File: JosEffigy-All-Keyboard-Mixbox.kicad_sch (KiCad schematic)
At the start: 33 parts, among them U1 Pico

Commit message: Release 1.0b
Moved power to VBUS, added DTranslator, added Capacitors
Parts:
- added C1, C10, C11, C12, C13, C14, C15, C16, C2, C3, C4, C5, C6, C7, C8, C9: 100nf, CAPC1005X55N:CAPC1005X55N, symbol Device:C_Small
- added U2: SN74LV1T34DBV, Package_TO_SOT_SMD:SOT-23-5, symbol Logic_LevelTranslator:SN74LV1T34DBV
- MX8: footprint Button_Switch_Keyboard:SW_Cherry_MX_2.00u_Plate -> PCM_Switch_Keyboard_Hotswap_Kailh:SW_Hotswap_Kailh_MX_Plated_2.00u
- U1: footprint RPi_Pico:RPi_Pico_SMD_TH -> MCU_RaspberryPi_and_Boards:RPi_Pico_SMD_TH
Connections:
- net GND: now also U1.38 (GND), C1.2, C10.2, C11.2, C12.2, C13.2, C14.2, C15.2, C16.2, C2.2, C3.2, C4.2, C5.2, C6.2, C7.2, C8.2, C9.2, U2.3 (GND)
- net RGB0: now also U2.2 (A); no longer D1.3 (DIN)
- net VCC: now also U1.40 (VBUS), C1.1, C10.1, C11.1, C12.1, C13.1, C14.1, C15.1, C16.1, C2.1, C3.1, C4.1, C5.1, C6.1, C7.1, C8.1, C9.1, U2.5 (VCC); no longer U1.36 (3V3)
- net at D13.1 (DOUT): no longer D14.3 (DIN)
- net at D13.3 (DIN): now also D14.1 (DOUT); no longer D12.1 (DOUT)
- net at D16.3 (DIN): now also D12.1 (DOUT); no longer D15.1 (DOUT)
- net at D15.3 (DIN): now also D16.1 (DOUT); no longer D14.1 (DOUT)
- new net: D1.3 (DIN), U2.4 (Y)
- new net: D14.3 (DIN), D15.1 (DOUT)

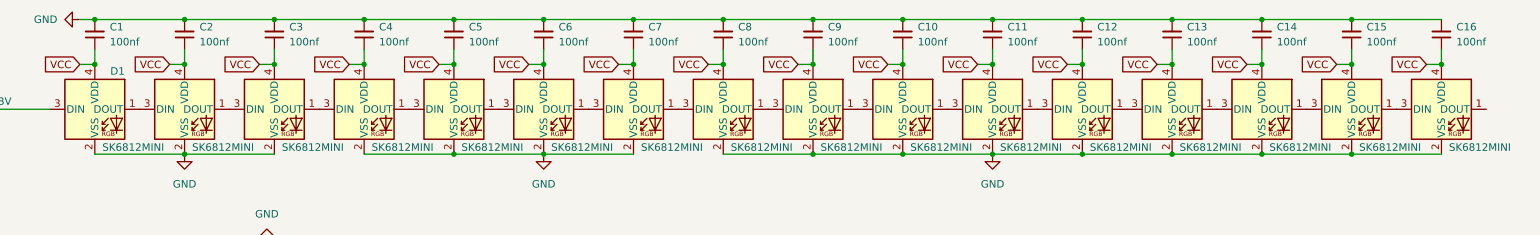
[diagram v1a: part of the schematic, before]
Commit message: Release 1.0c
redid the routing
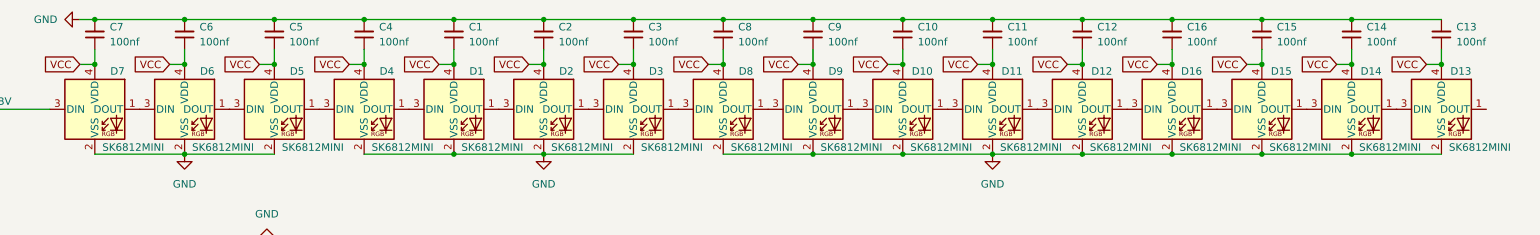
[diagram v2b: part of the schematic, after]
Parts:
- removed D7: SK6812MINI, kicad-footprints:YS-SK6812MINI-E, symbol LED:SK6812MINI
- added D1: SK6812MINI, kicad-footprints:YS-SK6812MINI-E, symbol LED:SK6812MINI
- renumbered C5 to C1, C16 to C13, C15 to C14, C14 to C15, C13 to C16, C6 to C2, C7 to C3, C3 to C5, C2 to C6, C1 to C7, D1 to D7
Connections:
- net GND: now also D1.2 (VSS)
- net VCC: now also D1.4 (VDD)
- net at D8.3 (DIN): now also D3.1 (DOUT)
- net at D7.1 (DOUT): now also D6.3 (DIN); no longer D2.3 (DIN)
- net at D5.3 (DIN): now also D6.1 (DOUT); no longer D4.1 (DOUT)
- net at D4.3 (DIN): now also D5.1 (DOUT); no longer D3.1 (DOUT)
- new net: D1.3 (DIN), D4.1 (DOUT)
- new net: D1.1 (DOUT), D2.3 (DIN)

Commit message: Release 1.1b
Update just to be sure
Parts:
- MX1, MX10, MX11, MX12, MX13, MX14, MX15, MX16, MX2, MX3, MX4, MX5, MX6, MX7, MX9: footprint PCM_Switch_Keyboard_Hotswap_Kailh:SW_Hotswap_Kailh_MX_Plated_1.00u -> Kailh:Kailh_socket_PG1350_optional
- MX8: footprint PCM_Switch_Keyboard_Hotswap_Kailh:SW_Hotswap_Kailh_MX_Plated_2.00u -> Kailh:Kailh_socket_PG1350_optional
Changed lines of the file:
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@@
       (effects (font (size 0.508 0.508)))
     )
-    (property "Footprint" "PCM_Switch_Keyboard_Hotswap_Kailh:SW_Hotswap_Kailh_MX_Plated_1.00u" (at 109.855 62.865 0)
+    (property "Footprint" "Kailh:Kailh_socket_PG1350_optional" (at 109.855 62.865 0)
       (effects (font (size 1.524 1.524)) hide)
     )
@@
       (effects (font (size 0.508 0.508)))
     )
-    (property "Footprint" "PCM_Switch_Keyboard_Hotswap_Kailh:SW_Hotswap_Kailh_MX_Plated_1.00u" (at 198.755 100.965 0)
+    (property "Footprint" "Kailh:Kailh_socket_PG1350_optional" (at 198.755 100.965 0)
       (effects (font (size 1.524 1.524)) hide)
     )
@@
       (effects (font (size 0.508 0.508)))
     )
-    (property "Footprint" "PCM_Switch_Keyboard_Hotswap_Kailh:SW_Hotswap_Kailh_MX_Plated_1.00u" (at 224.155 88.265 0)
+    (property "Footprint" "Kailh:Kailh_socket_PG1350_optional" (at 224.155 88.265 0)
       (effects (font (size 1.524 1.524)) hide)
     )
@@
       (effects (font (size 0.508 0.508)))
     )
-    (property "Footprint" "PCM_Switch_Keyboard_Hotswap_Kailh:SW_Hotswap_Kailh_MX_Plated_1.00u" (at 224.155 100.965 0)
+    (property "Footprint" "Kailh:Kailh_socket_PG1350_optional" (at 224.155 100.965 0)
       (effects (font (size 1.524 1.524)) hide)
     )
@@
       (effects (font (size 0.508 0.508)))
     )
-    (property "Footprint" "PCM_Switch_Keyboard_Hotswap_Kailh:SW_Hotswap_Kailh_MX_Plated_1.00u" (at 135.255 62.865 0)
+    (property "Footprint" "Kailh:Kailh_socket_PG1350_optional" (at 135.255 62.865 0)
       (effects (font (size 1.524 1.524)) hide)
     )
@@
       (effects (font (size 0.508 0.508)))
     )
-    (property "Footprint" "PCM_Switch_Keyboard_Hotswap_Kailh:SW_Hotswap_Kailh_MX_Plated_1.00u" (at 186.055 100.965 0)
+    (property "Footprint" "Kailh:Kailh_socket_PG1350_optional" (at 186.055 100.965 0)
       (effects (font (size 1.524 1.524)) hide)
     )
@@
       (effects (font (size 0.508 0.508)))
     )
-    (property "Footprint" "PCM_Switch_Keyboard_Hotswap_Kailh:SW_Hotswap_Kailh_MX_Plated_1.00u" (at 109.855 100.965 0)
+    (property "Footprint" "Kailh:Kailh_socket_PG1350_optional" (at 109.855 100.965 0)
       (effects (font (size 1.524 1.524)) hide)
     )
@@
       (effects (font (size 0.508 0.508)))
     )
-    (property "Footprint" "PCM_Switch_Keyboard_Hotswap_Kailh:SW_Hotswap_Kailh_MX_Plated_1.00u" (at 122.555 100.965 0)
+    (property "Footprint" "Kailh:Kailh_socket_PG1350_optional" (at 122.555 100.965 0)
       (effects (font (size 1.524 1.524)) hide)
     )
@@
       (effects (font (size 0.508 0.508)))
     )
-    (property "Footprint" "PCM_Switch_Keyboard_Hotswap_Kailh:SW_Hotswap_Kailh_MX_Plated_1.00u" (at 122.555 88.265 0)
+    (property "Footprint" "Kailh:Kailh_socket_PG1350_optional" (at 122.555 88.265 0)
       (effects (font (size 1.524 1.524)) hide)
     )
@@
       (effects (font (size 0.508 0.508)))
     )
-    (property "Footprint" "PCM_Switch_Keyboard_Hotswap_Kailh:SW_Hotswap_Kailh_MX_Plated_1.00u" (at 186.055 88.265 0)
+    (property "Footprint" "Kailh:Kailh_socket_PG1350_optional" (at 186.055 88.265 0)
       (effects (font (size 1.524 1.524)) hide)
     )
@@
       (effects (font (size 0.508 0.508)))
     )
-    (property "Footprint" "PCM_Switch_Keyboard_Hotswap_Kailh:SW_Hotswap_Kailh_MX_Plated_1.00u" (at 211.455 88.265 0)
+    (property "Footprint" "Kailh:Kailh_socket_PG1350_optional" (at 211.455 88.265 0)
       (effects (font (size 1.524 1.524)) hide)
     )
@@
       (effects (font (size 0.508 0.508)))
     )
-    (property "Footprint" "PCM_Switch_Keyboard_Hotswap_Kailh:SW_Hotswap_Kailh_MX_Plated_1.00u" (at 198.755 88.265 0)
+    (property "Footprint" "Kailh:Kailh_socket_PG1350_optional" (at 198.755 88.265 0)
       (effects (font (size 1.524 1.524)) hide)
     )
@@
       (effects (font (size 0.508 0.508)))
     )
-    (property "Footprint" "PCM_Switch_Keyboard_Hotswap_Kailh:SW_Hotswap_Kailh_MX_Plated_1.00u" (at 211.455 100.965 0)
+    (property "Footprint" "Kailh:Kailh_socket_PG1350_optional" (at 211.455 100.965 0)
       (effects (font (size 1.524 1.524)) hide)
     )
@@
       (effects (font (size 0.508 0.508)))
     )
-    (property "Footprint" "PCM_Switch_Keyboard_Hotswap_Kailh:SW_Hotswap_Kailh_MX_Plated_1.00u" (at 122.555 62.865 0)
+    (property "Footprint" "Kailh:Kailh_socket_PG1350_optional" (at 122.555 62.865 0)
       (effects (font (size 1.524 1.524)) hide)
     )
@@
       (effects (font (size 0.508 0.508)))
     )
-    (property "Footprint" "PCM_Switch_Keyboard_Hotswap_Kailh:SW_Hotswap_Kailh_MX_Plated_1.00u" (at 135.255 100.965 0)
+    (property "Footprint" "Kailh:Kailh_socket_PG1350_optional" (at 135.255 100.965 0)
       (effects (font (size 1.524 1.524)) hide)
     )
@@
       (effects (font (size 0.508 0.508)))
     )
-    (property "Footprint" "PCM_Switch_Keyboard_Hotswap_Kailh:SW_Hotswap_Kailh_MX_Plated_2.00u" (at 160.655 113.665 0)
-      (effects (font (size 1.524 1.524)) hide)
-    )
+    (property "Footprint" "Kailh:Kailh_socket_PG1350_optional" (at 160.655 113.665 0)
+      (effects (font (size 1.524 1.524)) hide)
+    )

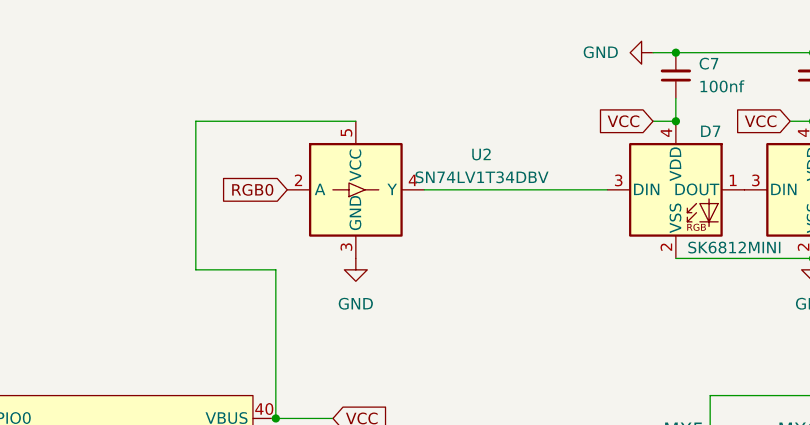
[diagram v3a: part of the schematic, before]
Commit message: Redid all routing manually
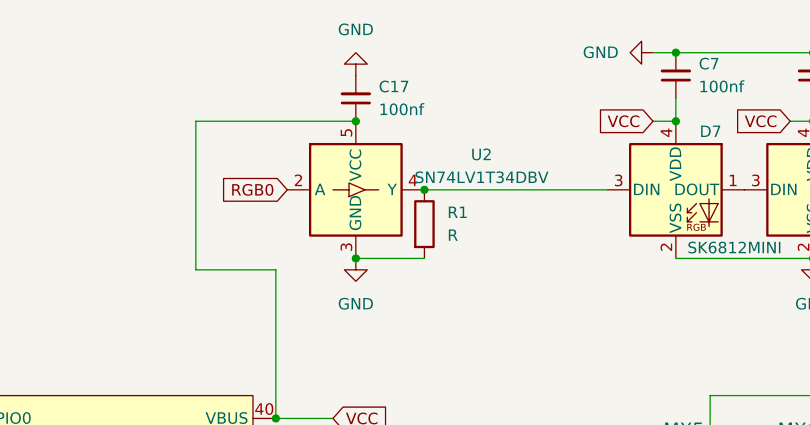
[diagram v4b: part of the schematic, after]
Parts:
- added C17: 100nf, CAPC1005X55N:CAPC1005X55N, symbol Device:C_Small
- added R1: R, Resistor_SMD:R_0402_1005Metric, symbol Device:R
- MX1, MX10, MX11, MX12, MX13, MX14, MX15, MX16, MX2, MX3, MX4, MX5, MX6, MX7, MX9: footprint Kailh:Kailh_socket_PG1350_optional -> PCM_Switch_Keyboard_Hotswap_Kailh:SW_Hotswap_Kailh_MX_Plated_1.00u
- MX8: footprint Kailh:Kailh_socket_PG1350_optional -> PCM_Switch_Keyboard_Hotswap_Kailh:SW_Hotswap_Kailh_MX_Plated_2.00u
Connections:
- net GND: now also C17.2, R1.2
- net VCC: now also C17.1
- net at D7.3 (DIN), U2.4 (Y): now also R1.1
